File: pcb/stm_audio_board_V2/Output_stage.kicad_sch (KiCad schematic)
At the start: 30 parts, among them U3 OP275, U6 OP275

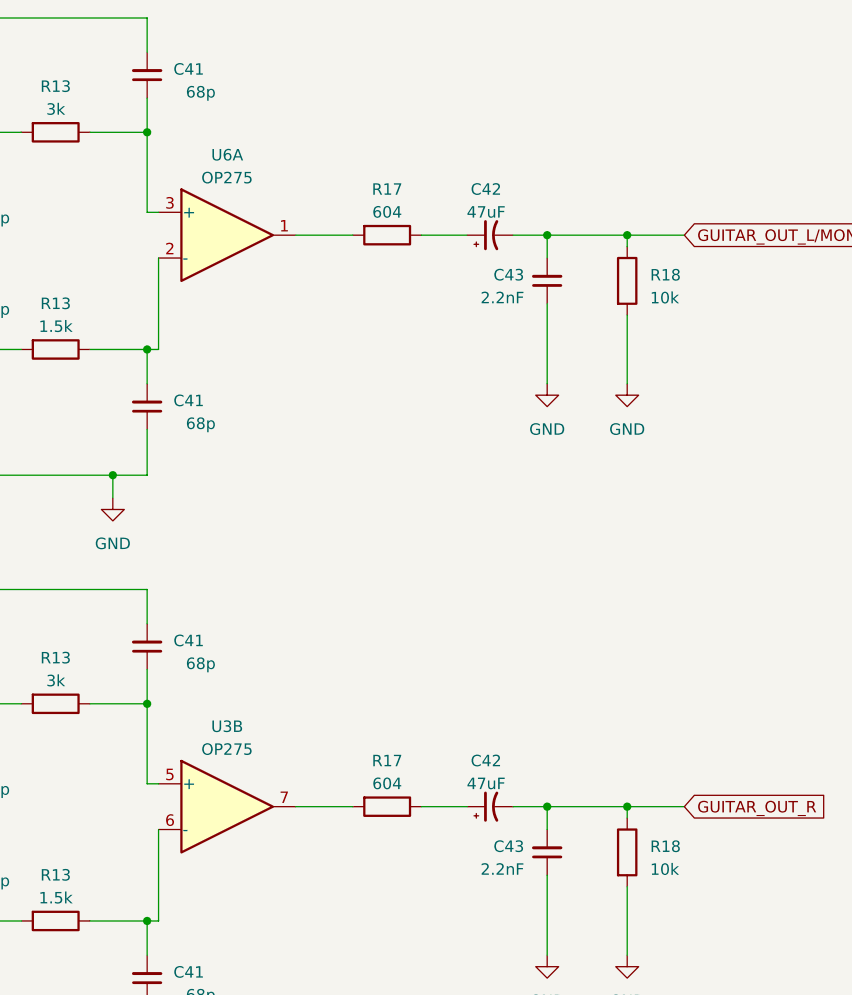
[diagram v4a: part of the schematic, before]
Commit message: PCB design started INPUT and OUTPUT stage done, codec placed
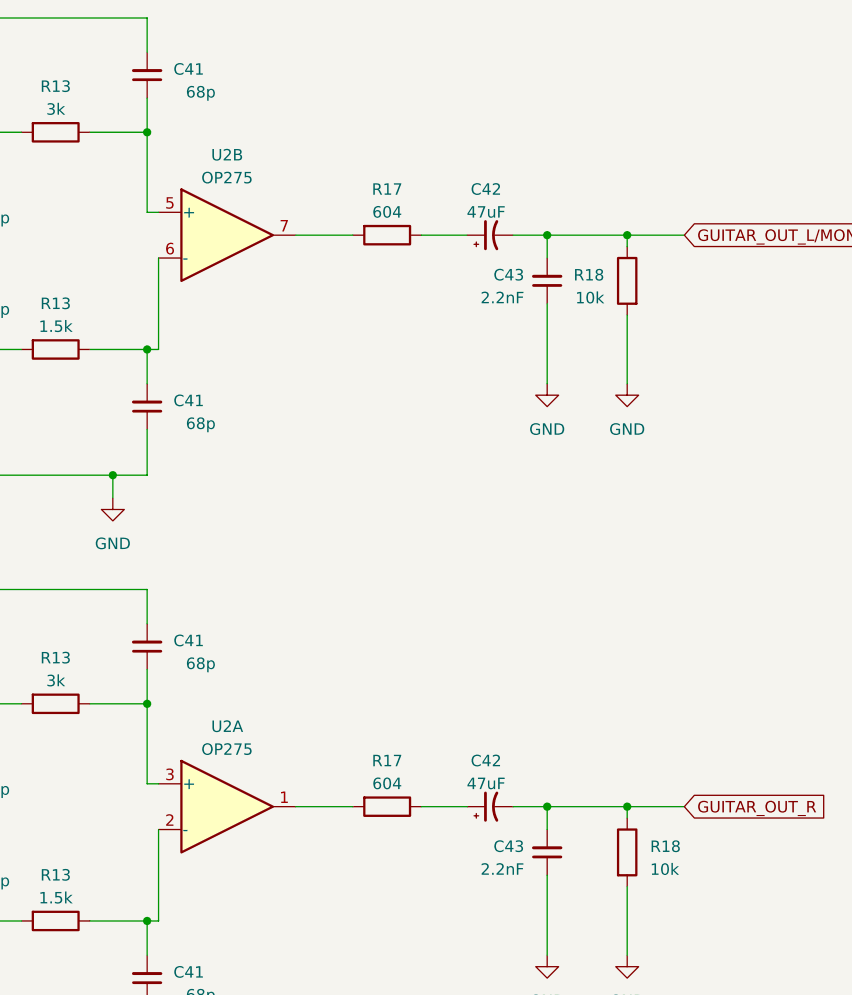
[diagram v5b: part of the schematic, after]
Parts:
- removed U3, U6: OP275, symbol Amplifier_Operational:OP275
- added U2: OP275, Package_SO:SSOP-8_3.9x5.05mm_P1.27mm, symbol Amplifier_Operational:OP275
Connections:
- net at R17.2: now also U2.7
- net at C41.2, R13.1: now also U2.6 (-)
- net at C41.1, R13.1: now also U2.5 (+)
- net at C41.1, R13.1: now also U2.3 (+)
- net at C41.2, R13.1: now also U2.2 (-)
- net at R17.2: now also U2.1

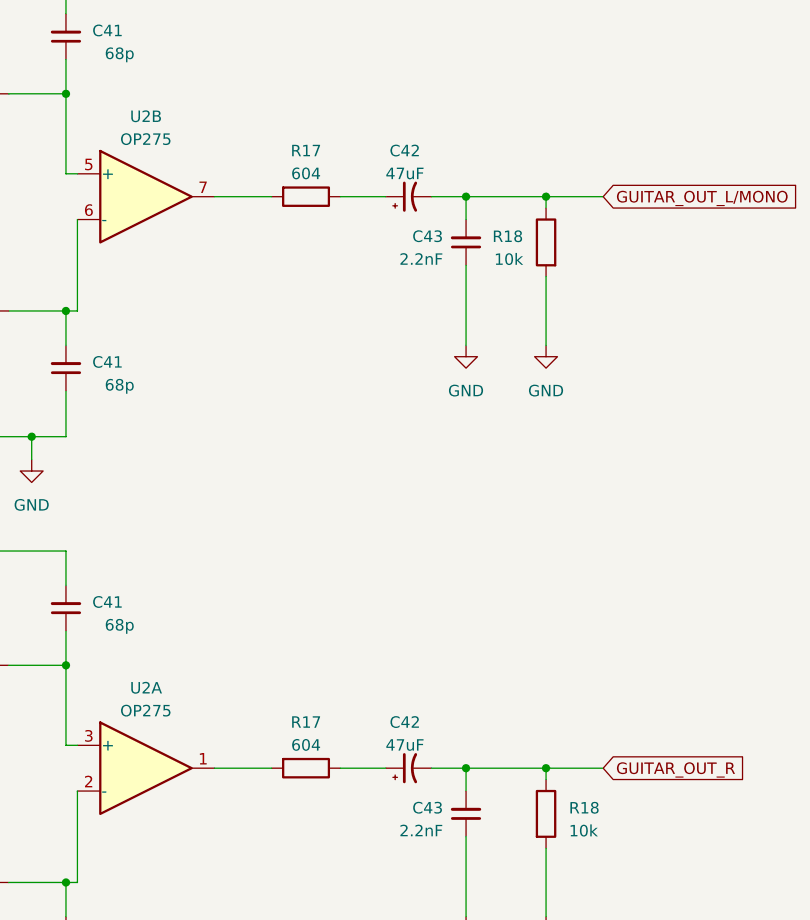
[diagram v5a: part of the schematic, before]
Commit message: silkscreen updated
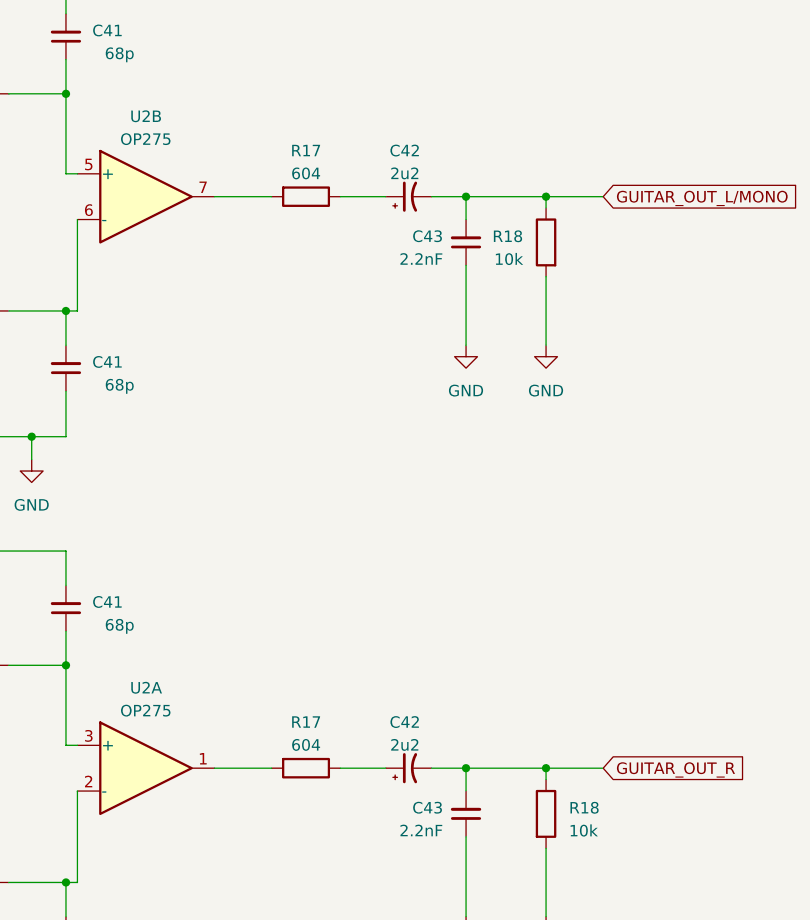
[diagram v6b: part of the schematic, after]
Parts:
- C42: value 47uF -> 2u2
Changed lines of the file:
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@@
       (effects (font (size 1.27 1.27)))
     )
-    (property "Value" "47uF" (at 153.2382 67.31 90)
+    (property "Value" "2u2" (at 153.2382 67.31 90)
       (effects (font (size 1.27 1.27)))
     )
@@
       (effects (font (size 1.27 1.27)))
     )
-    (property "Value" "47uF" (at 153.2382 130.81 90)
-      (effects (font (size 1.27 1.27)))
-    )
+    (property "Value" "2u2" (at 153.2382 130.81 90)
+      (effects (font (size 1.27 1.27)))
+    )

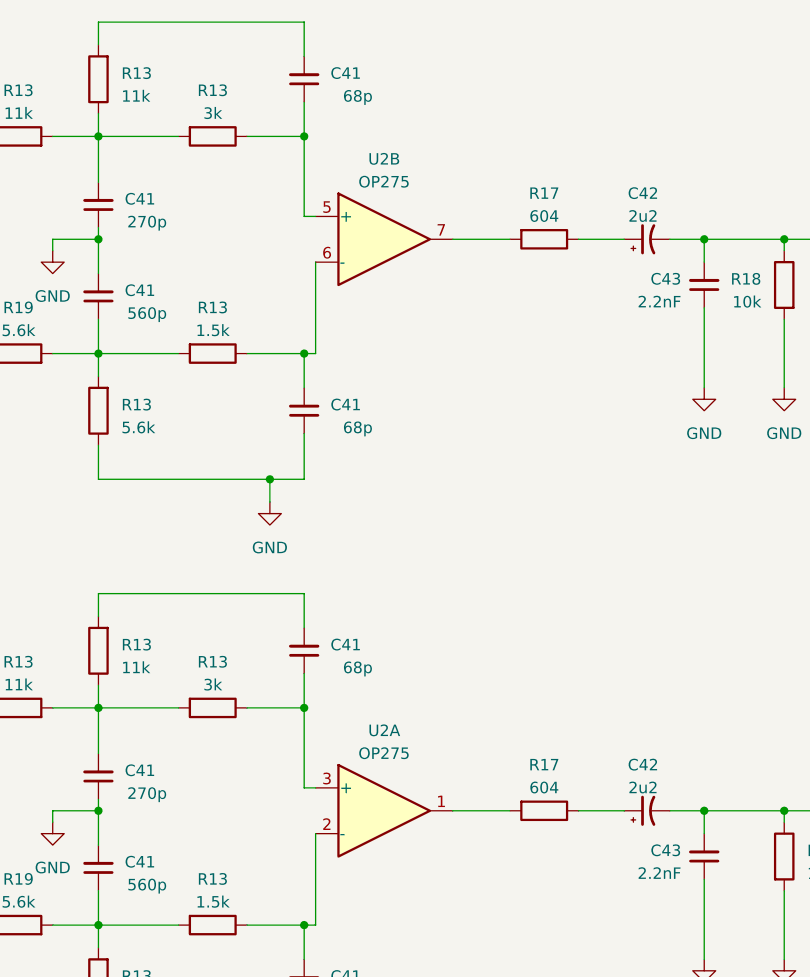
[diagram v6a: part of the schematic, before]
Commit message: added vias and overall fixes around pcb
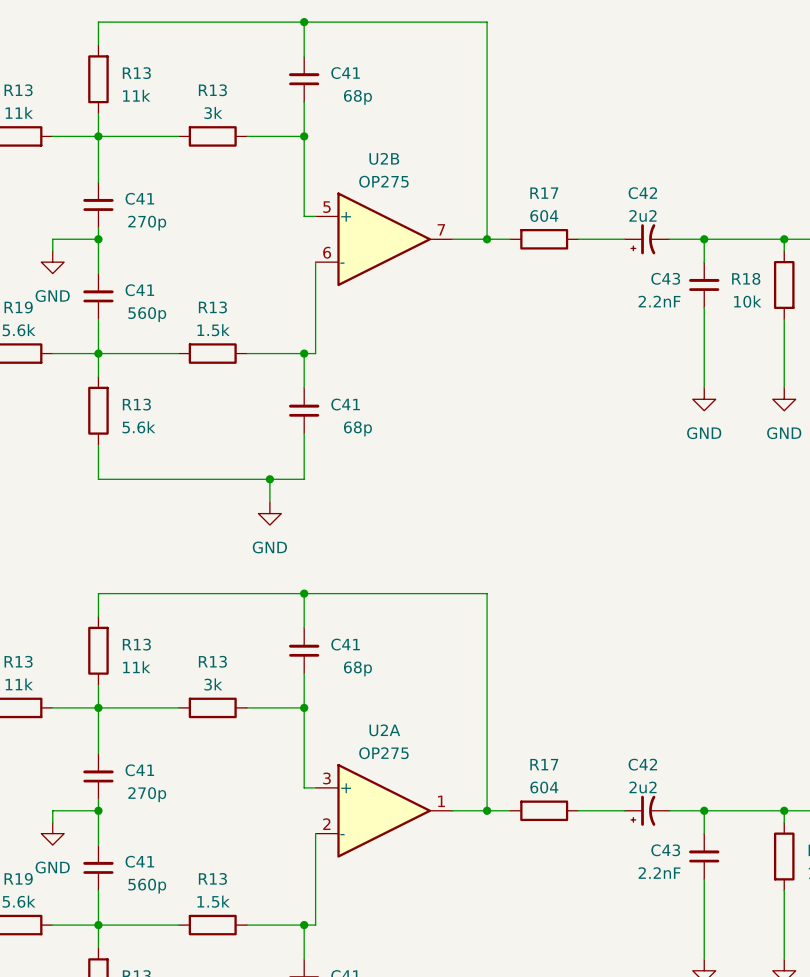
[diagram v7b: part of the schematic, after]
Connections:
- net at R17.2, U2.7: now also C41.2, R13.2
- net at R17.2, U2.1: now also C41.2, R13.2
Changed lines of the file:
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@@
 (kicad_sch (version 20230121) (generator eeschema)
   (paper "A4")
+  (junction (at 135.89 133.35) (diameter 0) (color 0 0 0 0)
+  )
   (junction (at 92.71 69.85) (diameter 0) (color 0 0 0 0)
   )
@@
   (junction (at 160.02 69.85) (diameter 0) (color 0 0 0 0)
   )
+  (junction (at 135.89 69.85) (diameter 0) (color 0 0 0 0)
+  )
   (junction (at 111.76 160.02) (diameter 0) (color 0 0 0 0)
   )
@@
   (junction (at 92.71 121.92) (diameter 0) (color 0 0 0 0)
   )
+  (junction (at 115.57 45.72) (diameter 0) (color 0 0 0 0)
+  )
   (junction (at 115.57 58.42) (diameter 0) (color 0 0 0 0)
   )
@@
   (junction (at 92.71 133.35) (diameter 0) (color 0 0 0 0)
   )
+  (junction (at 115.57 109.22) (diameter 0) (color 0 0 0 0)
+  )
   (junction (at 115.57 121.92) (diameter 0) (color 0 0 0 0)
   )
@@
     (stroke (width 0) (type default))
   )
+  (wire (pts (xy 135.89 133.35) (xy 138.43 133.35))
+    (stroke (width 0) (type default))
+  )
   (wire (pts (xy 146.05 133.35) (xy 151.13 133.35))
     (stroke (width 0) (type default))
@@
     (stroke (width 0) (type default))
   )
+  (wire (pts (xy 115.57 45.72) (xy 135.89 45.72))
+    (stroke (width 0) (type default))
+  )
   (wire (pts (xy 78.74 121.92) (xy 80.01 121.92))
     (stroke (width 0) (type default))
@@
     (stroke (width 0) (type default))
   )
-  (wire (pts (xy 132.08 69.85) (xy 138.43 69.85))
+  (wire (pts (xy 132.08 69.85) (xy 135.89 69.85))
     (stroke (width 0) (type default))
   )
@@
     (stroke (width 0) (type default))
   )
+  (wire (pts (xy 135.89 69.85) (xy 138.43 69.85))
+    (stroke (width 0) (type default))
+  )
+  (wire (pts (xy 135.89 45.72) (xy 135.89 69.85))
+    (stroke (width 0) (type default))
+  )
   (wire (pts (xy 92.71 142.24) (xy 92.71 146.05))
     (stroke (width 0) (type default))
@@
     (stroke (width 0) (type default))
   )
+  (wire (pts (xy 135.89 109.22) (xy 135.89 133.35))
+    (stroke (width 0) (type default))
+  )
   (wire (pts (xy 87.63 121.92) (xy 92.71 121.92))
     (stroke (width 0) (type default))
@@
     (stroke (width 0) (type default))
   )
-  (wire (pts (xy 132.08 133.35) (xy 138.43 133.35))
+  (wire (pts (xy 132.08 133.35) (xy 135.89 133.35))
     (stroke (width 0) (type default))
   )
@@
     (stroke (width 0) (type default))
   )
+  (wire (pts (xy 115.57 109.22) (xy 135.89 109.22))
+    (stroke (width 0) (type default))
+  )

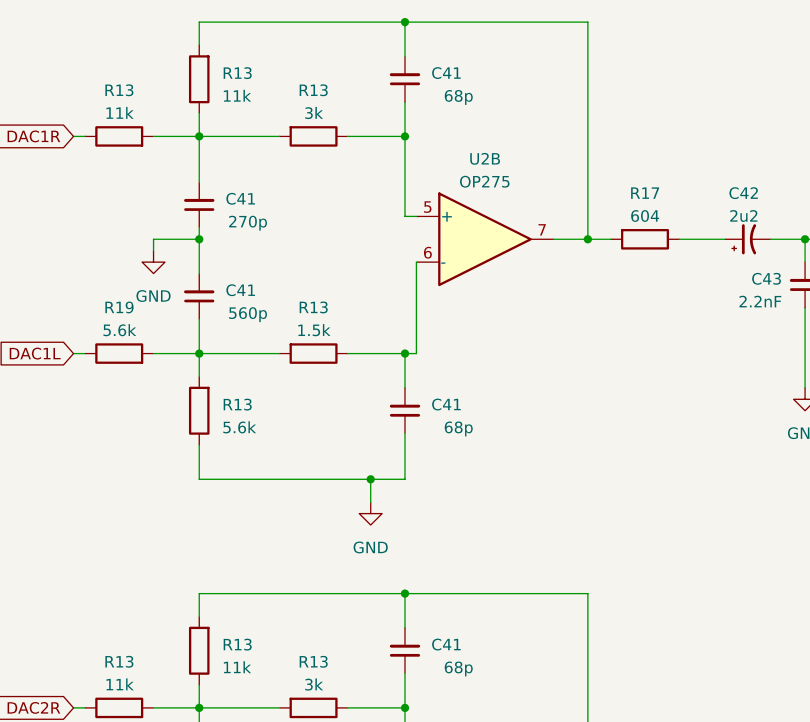
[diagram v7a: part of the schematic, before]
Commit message: First working project
The AD1939 PLL loop changed for DBCLK pll input, the ad1939 now works as a slave, the stm32 i2s interfaces are masters (errata). The PLL loop needs VDD not GND!!!!
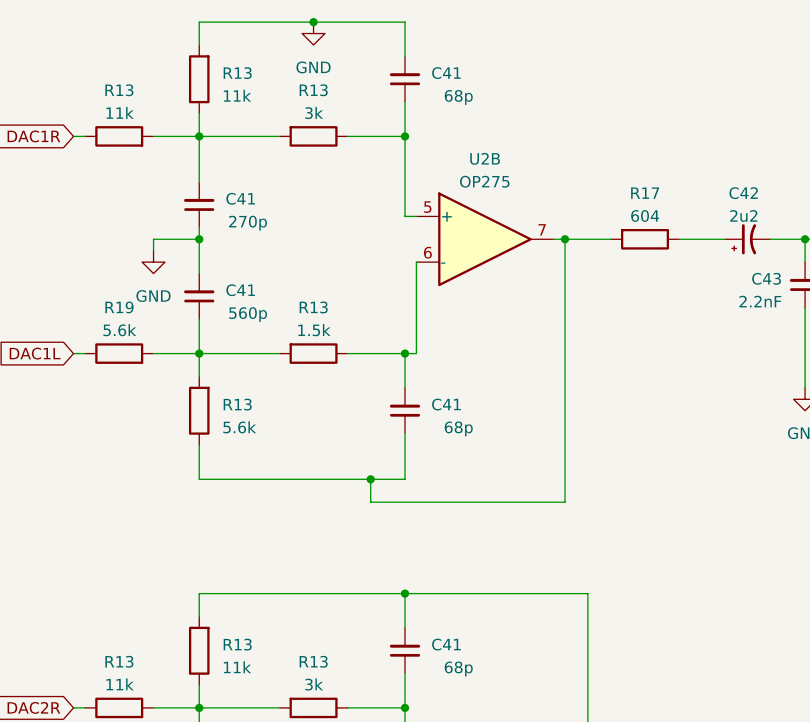
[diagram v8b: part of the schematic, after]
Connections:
- net GND: now also C41.2, R13.2; no longer C41.1, R13.1
- net at R17.2, U2.7: now also C41.1, R13.1; no longer C41.2, R13.2
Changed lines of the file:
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@@
   (junction (at 160.02 69.85) (diameter 0) (color 0 0 0 0)
   )
-  (junction (at 135.89 69.85) (diameter 0) (color 0 0 0 0)
-  )
   (junction (at 111.76 160.02) (diameter 0) (color 0 0 0 0)
   )
@@
   (junction (at 92.71 121.92) (diameter 0) (color 0 0 0 0)
   )
-  (junction (at 115.57 45.72) (diameter 0) (color 0 0 0 0)
-  )
   (junction (at 115.57 58.42) (diameter 0) (color 0 0 0 0)
   )
+  (junction (at 105.41 45.72) (diameter 0) (color 0 0 0 0)
+  )
   (junction (at 160.02 133.35) (diameter 0) (color 0 0 0 0)
   )
+  (junction (at 133.35 69.85) (diameter 0) (color 0 0 0 0)
+  )
   (junction (at 168.91 69.85) (diameter 0) (color 0 0 0 0)
   )
@@
     (stroke (width 0) (type default))
   )
-  (wire (pts (xy 92.71 45.72) (xy 115.57 45.72))
+  (wire (pts (xy 92.71 45.72) (xy 105.41 45.72))
     (stroke (width 0) (type default))
   )
@@
     (stroke (width 0) (type default))
   )
-  (wire (pts (xy 115.57 45.72) (xy 135.89 45.72))
-    (stroke (width 0) (type default))
-  )
   (wire (pts (xy 78.74 121.92) (xy 80.01 121.92))
     (stroke (width 0) (type default))
@@
     (stroke (width 0) (type default))
   )
-  (wire (pts (xy 132.08 69.85) (xy 135.89 69.85))
+  (wire (pts (xy 132.08 69.85) (xy 133.35 69.85))
     (stroke (width 0) (type default))
   )
@@
     (stroke (width 0) (type default))
   )
-  (wire (pts (xy 135.89 69.85) (xy 138.43 69.85))
-    (stroke (width 0) (type default))
-  )
-  (wire (pts (xy 135.89 45.72) (xy 135.89 69.85))
-    (stroke (width 0) (type default))
-  )
   (wire (pts (xy 92.71 142.24) (xy 92.71 146.05))
     (stroke (width 0) (type default))
@@
     (stroke (width 0) (type default))
   )
+  (wire (pts (xy 105.41 45.72) (xy 115.57 45.72))
+    (stroke (width 0) (type default))
+  )
   (wire (pts (xy 135.89 109.22) (xy 135.89 133.35))
     (stroke (width 0) (type default))
   )
+  (wire (pts (xy 111.76 99.06) (xy 133.35 99.06))
+    (stroke (width 0) (type default))
+  )
   (wire (pts (xy 87.63 121.92) (xy 92.71 121.92))
     (stroke (width 0) (type default))
   )
+  (wire (pts (xy 133.35 99.06) (xy 133.35 69.85))
+    (stroke (width 0) (type default))
+  )
   (wire (pts (xy 115.57 82.55) (xy 116.84 82.55))
     (stroke (width 0) (type default))
@@
   )
   (wire (pts (xy 115.57 67.31) (xy 115.57 58.42))
+    (stroke (width 0) (type default))
+  )
+  (wire (pts (xy 133.35 69.85) (xy 138.43 69.85))
     (stroke (width 0) (type default))
   )
@@
     )
   )
-  (symbol (lib_id "power:GND") (at 111.76 99.06 0) (unit 1)
-    (in_bom yes) (on_board yes) (dnp no) (fields_autoplaced)
-    (property "Reference" "#PWR02" (at 111.76 105.41 0)
-      (effects (font (size 1.27 1.27)) hide)
-    )
-    (property "Value" "GND" (at 111.76 104.14 0)
-      (effects (font (size 1.27 1.27)))
-    )
-    (property "Footprint" "" (at 111.76 99.06 0)
-      (effects (font (size 1.27 1.27)) hide)
-    )
-    (property "Datasheet" "" (at 111.76 99.06 0)
-      (effects (font (size 1.27 1.27)) hide)
-    )
-    (pin "1")
-    (instances
-      (project "stm_audio_board_V2"
-        (path "/6997cf63-2615-4e49-9471-e7da1b6bae71"
-          (reference "#PWR02") (unit 1)
-        )
-        (path "/6997cf63-2615-4e49-9471-e7da1b6bae71/2eb2ee8f-ab98-4666-97f0-bfacb073bc88"
-          (reference "#PWR01") (unit 1)
-        )
-        (path "/6997cf63-2615-4e49-9471-e7da1b6bae71/83920463-7bb1-4088-aad8-702bcdea14ea"
-          (reference "#PWR015") (unit 1)
-        )
-      )
-    )
-  )
   (symbol (lib_id "Device:R") (at 83.82 82.55 90) (unit 1)
     (in_bom yes) (on_board yes) (dnp no) (fields_autoplaced)
@@
         )
       )
+    )
+  )
+  (symbol (lib_id "power:GND") (at 105.41 45.72 0) (unit 1)
+    (in_bom yes) (on_board yes) (dnp no) (fields_autoplaced)
+    (property "Reference" "#PWR02" (at 105.41 52.07 0)
+      (effects (font (size 1.27 1.27)) hide)
+    )
+    (property "Value" "GND" (at 105.41 50.8 0)
+      (effects (font (size 1.27 1.27)))
+    )
+    (property "Footprint" "" (at 105.41 45.72 0)
+      (effects (font (size 1.27 1.27)) hide)
+    )
+    (property "Datasheet" "" (at 105.41 45.72 0)
+      (effects (font (size 1.27 1.27)) hide)
+    )
+    (pin "1")
+    (instances
+      (project "stm_audio_board_V2"
+        (path "/6997cf63-2615-4e49-9471-e7da1b6bae71"
+          (reference "#PWR02") (unit 1)
+        )
+        (path "/6997cf63-2615-4e49-9471-e7da1b6bae71/2eb2ee8f-ab98-4666-97f0-bfacb073bc88"
+          (reference "#PWR01") (unit 1)
+        )
+        (path "/6997cf63-2615-4e49-9471-e7da1b6bae71/83920463-7bb1-4088-aad8-702bcdea14ea"
+          (reference "#PWR015") (unit 1)
+        )
+      )
